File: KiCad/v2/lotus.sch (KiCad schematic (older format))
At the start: 32 parts, among them IC1 DW01A-G, J1 USB_OTG, J2 FTDI, Q1 FS8205A, SW1 SW_Push, SW2 SW_DIP_x01, SW3 SW_Push, U1 LD1117S33CTR, U2 TP4056, U3 ESP-12E

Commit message: Atualizado versão 2
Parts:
- removed BT1: Battery_Cell, Pin_Headers:Pin_Header_Straight_1x02_Pitch2.54mm, symbol Battery_Cell
- removed C1: 10u, Capacitors_SMD:C_0402, symbol C
- removed C2, C3: 0.1u, Capacitors_SMD:C_0402, symbol C
- removed C4, C5: 100n, Capacitors_SMD:C_0402, symbol C
- removed C6: 100n, Capacitors_Tantalum_SMD:CP_Tantalum_Case-C_EIA-6032-28_Hand, symbol CP1
- removed C7: 10u, Capacitors_Tantalum_SMD:CP_Tantalum_Case-C_EIA-6032-28_Hand, symbol CP1
- removed D1: LED_ARGB, LEDs:LED_D5.0mm-4, symbol LED_ARGB
- removed IC1: DW01A-G, DW01A-G:SOT95P190X145-6N, symbol DW01A-G
- removed J1: USB_OTG, Connectors:USB_Micro-B, symbol USB_OTG
- removed J2: FTDI, Pin_Headers:Pin_Header_Straight_1x04_Pitch2.54mm, symbol CONN_01X04
- removed Q1: FS8205A, FS8205A:SOP65P640X120-8N, symbol FS8205A
- removed R1, R2, R6: 1k, Resistors_SMD:R_0402, symbol R
- removed R10, R11, R12, R13, R4, R7, R8, R9: 10k, Resistors_SMD:R_0402, symbol R
- removed R3: 1.2k, Resistors_SMD:R_0402, symbol R
- removed R5: 100, Resistors_SMD:R_0402, symbol R
- removed SW1, SW3: SW_Push, Buttons_Switches_THT:SW_PUSH_6mm, symbol SW_Push
- removed SW2: SW_DIP_x01, Buttons_Switches_SMD:SW_DIP_x1_W5.08mm_Slide_Copal_CHS-A, symbol SW_DIP_x01-RESCUE-lotus
- removed U1: LD1117S33CTR, TO_SOT_Packages_SMD:SOT-223, symbol LD1117S33CTR
- removed U2: TP4056, TP4056:TP4056, symbol TP4056-RESCUE-lotus
- removed U3: ESP-12E, RF_Modules:ESP-12E, symbol ESP-12E
- added C? (x2): 100n, symbol Device:C
- added C?: 100n, symbol Device:CP1
- added C?: 10u, symbol Device:CP1
- added C?: 4.7u, symbol Device:C
- added C?: 1u, symbol Device:C
- added D?: LED_ARGB, symbol Device:LED_ARGB
- added J?: Conn_01x04, symbol Connector_Generic:Conn_01x04
- added J?: USB_B_Micro, symbol Connector:USB_B_Micro
- added R? (x6): 10k, symbol Device:R
- added R? (x2): 1.5k, symbol Device:R
- added R?: 1.13k, symbol Device:R
- added R?: 1.18k, symbol Device:R
- added SW? (x2): SW_Push, symbol Switch:SW_Push
- added SW?: SW_DIP_x01, symbol Switch:SW_DIP_x01
- added U?: ESP-12E, RF_Module:ESP-12E, symbol RF_Module:ESP-12E
- added U?: BQ24075, symbol Battery_Management:BQ24075
- added U?: LD1117S33TR_SOT223, Package_TO_SOT_SMD:SOT-223-3_TabPin2, symbol Regulator_Linear:LD1117S33TR_SOT223
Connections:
- net labels added: BAT, CHG, COLOR_BUTTON, LED_B, LED_G, LED_R, OUT, PGOOD, RST_BUTTON, TS_BAT
- net labels removed: LED_BUTTON, REST_BUTTON, led_b, led_g, led_r, pin_chrg, pin_stdby
- wire segments 103 -> 120
- no-connect marks 14 -> 7

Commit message: Adicionado bateria no esquemático v2
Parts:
- added C?: 4.7u, symbol Device:C
- added R?: 46.4k, symbol Device:R
- added R? (x2): 1.5k, symbol Device:R
- added U?: Battery, symbol Utils:Battery
- U?: value BQ24075 -> BQ24072; symbol Battery_Management:BQ24075 -> Battery_Management:BQ24072
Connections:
- wire segments 120 -> 136
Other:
- note added: "System"
- moved on the sheet: C?, D?, J?, R?, SW?, U?

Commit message: Mudado regulador de tensão
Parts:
- removed SW?: SW_DIP_x01, symbol Switch:SW_DIP_x01
- removed U?: LD1117S33TR_SOT223, Package_TO_SOT_SMD:SOT-223-3_TabPin2, symbol Regulator_Linear:LD1117S33TR_SOT223
- added J3: Conn_01x02, symbol Connector_Generic:Conn_01x02
- added U3: MIC5504-3.3YM5, Package_TO_SOT_SMD:SOT-23-5, symbol Regulator_Linear:MIC5504-3.3YM5
- C5: renamed from C?; value 100n -> 1u
- C6: renamed from C?; value 10u -> 1u
- gave numbers to parts that had none: 26
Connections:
- wire segments 136 -> 138
- no-connect marks 7 -> 11
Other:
- moved on the sheet: C5, C6

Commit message: Adicionado alguns footprints
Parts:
- C1, C2, C3, C4, C7: footprint (none) -> Capacitors_SMD:C_0402
- D1: footprint (none) -> LEDs:LED_Cree-PLCC4_3.2x2.8mm_CCW
- J1: footprint (none) -> Connectors:USB_Micro-B
- R1, R10, R11, R12, R13, R2, R3, R4, R5, R6, R7, R8, R9: footprint (none) -> Resistors_SMD:R_0402
- U1: footprint (none) -> Housings_DFN_QFN:QFN-16-1EP_3x3mm_Pitch0.5mm
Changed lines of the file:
@@
 F 0 "C1" H 2115 4846 50  0000 L CNN
 F 1 "100n" H 2115 4755 50  0000 L CNN
-F 2 "" H 2038 4650 50  0001 C CNN
+F 2 "Capacitors_SMD:C_0402" H 2038 4650 50  0001 C CNN
 F 3 "~" H 2000 4800 50  0001 C CNN
 	1    2000 4800
@@
 F 0 "R1" H 1870 4246 50  0000 L CNN
 F 1 "10k" H 1870 4155 50  0000 L CNN
-F 2 "" V 1730 4200 50  0001 C CNN
+F 2 "Resistors_SMD:R_0402" V 1730 4200 50  0001 C CNN
 F 3 "~" H 1800 4200 50  0001 C CNN
 	1    1800 4200
@@
 F 0 "R6" H 4120 4696 50  0000 L CNN
 F 1 "10k" H 4120 4605 50  0000 L CNN
-F 2 "" V 3980 4650 50  0001 C CNN
+F 2 "Resistors_SMD:R_0402" V 3980 4650 50  0001 C CNN
 F 3 "~" H 4050 4650 50  0001 C CNN
 	1    4050 4650
@@
 F 0 "R9" H 6520 5746 50  0000 L CNN
 F 1 "10k" H 6520 5655 50  0000 L CNN
-F 2 "" V 6380 5700 50  0001 C CNN
+F 2 "Resistors_SMD:R_0402" V 6380 5700 50  0001 C CNN
 F 3 "~" H 6450 5700 50  0001 C CNN
 	1    6450 5700
@@
 F 0 "R10" H 6570 4446 50  0000 L CNN
 F 1 "10k" H 6570 4355 50  0000 L CNN
-F 2 "" V 6430 4400 50  0001 C CNN
+F 2 "Resistors_SMD:R_0402" V 6430 4400 50  0001 C CNN
 F 3 "~" H 6500 4400 50  0001 C CNN
 	1    6500 4400
@@
 F 0 "R11" H 6920 4446 50  0000 L CNN
 F 1 "10k" H 6920 4355 50  0000 L CNN
-F 2 "" V 6780 4400 50  0001 C CNN
+F 2 "Resistors_SMD:R_0402" V 6780 4400 50  0001 C CNN
 F 3 "~" H 6850 4400 50  0001 C CNN
 	1    6850 4400
@@
 F 0 "D1" H 1800 6497 50  0000 C CNN
 F 1 "LED_ARGB" H 1800 6406 50  0000 C CNN
-F 2 "" H 1800 5950 50  0001 C CNN
+F 2 "LEDs:LED_Cree-PLCC4_3.2x2.8mm_CCW" H 1800 5950 50  0001 C CNN
 F 3 "~" H 1800 5950 50  0001 C CNN
 	1    1800 6000
@@
 F 0 "C3" H 3365 4846 50  0000 L CNN
 F 1 "100n" H 3365 4755 50  0000 L CNN
-F 2 "" H 3288 4650 50  0001 C CNN
+F 2 "Capacitors_SMD:C_0402" H 3288 4650 50  0001 C CNN
 F 3 "~" H 3250 4800 50  0001 C CNN
 	1    3250 4800
@@
 F 0 "R2" H 3120 4246 50  0000 L CNN
 F 1 "10k" H 3120 4155 50  0000 L CNN
-F 2 "" V 2980 4200 50  0001 C CNN
+F 2 "Resistors_SMD:R_0402" V 2980 4200 50  0001 C CNN
 F 3 "~" H 3050 4200 50  0001 C CNN
 	1    3050 4200
@@
 F 0 "U1" H 4400 2878 50  0000 C CNN
 F 1 "BQ24072" H 4400 2787 50  0000 C CNN
-F 2 "" H 4650 1550 50  0001 L CNN
+F 2 "Housings_DFN_QFN:QFN-16-1EP_3x3mm_Pitch0.5mm" H 4650 1550 50  0001 L CNN
 F 3 "http://www.ti.com/lit/ds/symlink/bq24075.pdf" H 4600 2300 50  0001 C CNN
 	1    4400 2100
@@
 F 0 "R7" V 5593 2400 50  0000 C CNN
 F 1 "1.5k" V 5684 2400 50  0000 C CNN
-F 2 "" V 5730 2400 50  0001 C CNN
+F 2 "Resistors_SMD:R_0402" V 5730 2400 50  0001 C CNN
 F 3 "~" H 5800 2400 50  0001 C CNN
 	1    5800 2400
@@
 F 0 "R8" V 5600 2500 50  0000 C CNN
 F 1 "1.5k" V 5700 2500 50  0000 C CNN
-F 2 "" V 5730 2500 50  0001 C CNN
+F 2 "Resistors_SMD:R_0402" V 5730 2500 50  0001 C CNN
 F 3 "~" H 5800 2500 50  0001 C CNN
 	1    5800 2500
@@
 F 0 "C4" H 5615 1946 50  0000 L CNN
 F 1 "4.7u" H 5615 1855 50  0000 L CNN
-F 2 "" H 5538 1750 50  0001 C CNN
+F 2 "Capacitors_SMD:C_0402" H 5538 1750 50  0001 C CNN
 F 3 "~" H 5500 1900 50  0001 C CNN
 	1    5500 1900
@@
 F 0 "C2" H 2600 2100 50  0000 L CNN
 F 1 "1u" H 2600 2000 50  0000 L CNN
-F 2 "" H 2838 1900 50  0001 C CNN
+F 2 "Capacitors_SMD:C_0402" H 2838 1900 50  0001 C CNN
 F 3 "~" H 2800 2050 50  0001 C CNN
 	1    2800 2050
@@
 F 0 "R5" H 3820 2796 50  0000 L CNN
 F 1 "1.13k" H 3820 2705 50  0000 L CNN
-F 2 "" V 3680 2750 50  0001 C CNN
+F 2 "Resistors_SMD:R_0402" V 3680 2750 50  0001 C CNN
 F 3 "~" H 3750 2750 50  0001 C CNN
 	1    3750 2750
@@
 F 0 "R4" H 3450 2800 50  0000 L CNN
 F 1 "1.18k" H 3350 2700 50  0000 L CNN
-F 2 "" V 3530 2750 50  0001 C CNN
+F 2 "Resistors_SMD:R_0402" V 3530 2750 50  0001 C CNN
 F 3 "~" H 3600 2750 50  0001 C CNN
 	1    3600 2750
@@
 F 0 "J1" H 2005 2417 50  0000 C CNN
 F 1 "USB_B_Micro" H 2005 2326 50  0000 C CNN
-F 2 "" H 2100 1900 50  0001 C CNN
+F 2 "Connectors:USB_Micro-B" H 2100 1900 50  0001 C CNN
 F 3 "~" H 2100 1900 50  0001 C CNN
 	1    1950 1950
@@
 F 0 "R3" H 3050 2200 50  0000 L CNN
 F 1 "46.4k" H 2950 2100 50  0000 L CNN
-F 2 "" V 3130 2150 50  0001 C CNN
+F 2 "Resistors_SMD:R_0402" V 3130 2150 50  0001 C CNN
 F 3 "~" H 3200 2150 50  0001 C CNN
 	1    3200 2150
@@
 F 0 "C7" H 9515 1696 50  0000 L CNN
 F 1 "4.7u" H 9515 1605 50  0000 L CNN
-F 2 "" H 9438 1500 50  0001 C CNN
+F 2 "Capacitors_SMD:C_0402" H 9438 1500 50  0001 C CNN
 F 3 "~" H 9400 1650 50  0001 C CNN
 	1    9400 1650
@@
 F 0 "R13" V 8650 2350 50  0000 C CNN
 F 1 "1.5k" V 8750 2350 50  0000 C CNN
-F 2 "" V 8780 2350 50  0001 C CNN
+F 2 "Resistors_SMD:R_0402" V 8780 2350 50  0001 C CNN
 F 3 "~" H 8850 2350 50  0001 C CNN
 	1    8850 2350
@@
 F 0 "R12" V 8350 2100 50  0000 C CNN
 F 1 "1.5k" V 8450 2100 50  0000 C CNN
-F 2 "" V 8480 2100 50  0001 C CNN
+F 2 "Resistors_SMD:R_0402" V 8480 2100 50  0001 C CNN
 F 3 "~" H 8550 2100 50  0001 C CNN
 	1    8550 2100

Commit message: Adicionado footprint dos botões, da bateria e dos conectores
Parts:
- C5, C6: footprint (none) -> Capacitors_Tantalum_SMD:CP_Tantalum_Case-A_EIA-3216-18_Hand
- J2: footprint (none) -> Connectors_JST:JST_JWPF_B04B-JWPF-SK-R_1x04_P2.00mm_Vertical
- SW1: footprint (none) -> Buttons_Switches_THT:SW_Tactile_SPST_Angled_PTS645Vx58-2LFS
- SW2: footprint (none) -> Buttons_Switches_THT:SW_PUSH_6mm
- U1: symbol Battery_Management:BQ24072 -> Lotus-rescue:BQ24072-Battery_Management
- U4: footprint (none) -> Pin_Headers:Pin_Header_Straight_1x03_Pitch2.54mm
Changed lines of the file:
@@
 EESchema Schematic File Version 4
 LIBS:Lotus-cache
-EELAYER 26 0
+EELAYER 29 0
 EELAYER END
 $Descr A4 11693 8268
@@
 F 0 "SW1" H 1800 4950 50  0000 R CNN
 F 1 "SW_Push" H 1750 4700 50  0000 R CNN
-F 2 "" H 1600 5000 50  0001 C CNN
+F 2 "Buttons_Switches_THT:SW_Tactile_SPST_Angled_PTS645Vx58-2LFS" H 1600 5000 50  0001 C CNN
 F 3 "" H 1600 5000 50  0001 C CNN
 	1    1600 4800
@@
 F 0 "SW2" H 3050 4950 50  0000 R CNN
 F 1 "SW_Push" H 3000 4700 50  0000 R CNN
-F 2 "" H 2850 5000 50  0001 C CNN
+F 2 "Buttons_Switches_THT:SW_PUSH_6mm" H 2850 5000 50  0001 C CNN
 F 3 "" H 2850 5000 50  0001 C CNN
 	1    2850 4800
@@
 F 0 "J2" H 2870 5575 50  0000 C CNN
 F 1 "Conn_01x04" H 2870 5666 50  0000 C CNN
-F 2 "" H 2950 6000 50  0001 C CNN
+F 2 "Connectors_JST:JST_JWPF_B04B-JWPF-SK-R_1x04_P2.00mm_Vertical" H 2950 6000 50  0001 C CNN
 F 3 "~" H 2950 6000 50  0001 C CNN
 	1    2950 6000
@@
 	2150 6000 2000 6000
 $Comp
-L Battery_Management:BQ24072 U1
+L Lotus-rescue:BQ24072-Battery_Management U1
 U 1 1 5BDC7AE2
 P 4400 2100
@@
 F 0 "C5" H 6665 2146 50  0000 L CNN
 F 1 "1u" H 6665 2055 50  0000 L CNN
-F 2 "" H 6550 2100 50  0001 C CNN
+F 2 "Capacitors_Tantalum_SMD:CP_Tantalum_Case-A_EIA-3216-18_Hand" H 6550 2100 50  0001 C CNN
 F 3 "~" H 6550 2100 50  0001 C CNN
 	1    6550 2100
@@
 F 0 "C6" H 7765 2146 50  0000 L CNN
 F 1 "1u" H 7765 2055 50  0000 L CNN
-F 2 "" H 7650 2100 50  0001 C CNN
+F 2 "Capacitors_Tantalum_SMD:CP_Tantalum_Case-A_EIA-3216-18_Hand" H 7650 2100 50  0001 C CNN
 F 3 "~" H 7650 2100 50  0001 C CNN
 	1    7650 2100
@@
 F 0 "U4" H 9477 2396 50  0000 L CNN
 F 1 "Battery" H 9477 2305 50  0000 L CNN
-F 2 "" H 9250 2300 50  0001 C CNN
+F 2 "Pin_Headers:Pin_Header_Straight_1x03_Pitch2.54mm" H 9250 2300 50  0001 C CNN
 F 3 "" H 9250 2300 50  0001 C CNN
 	1    9250 2300

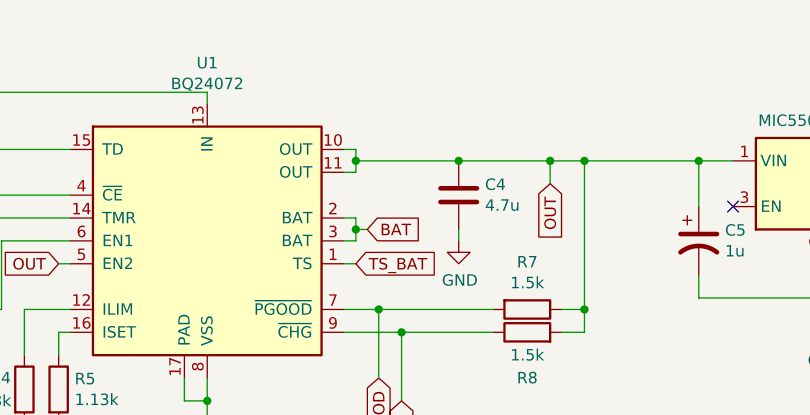
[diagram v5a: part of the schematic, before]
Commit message: Atualizado footprints
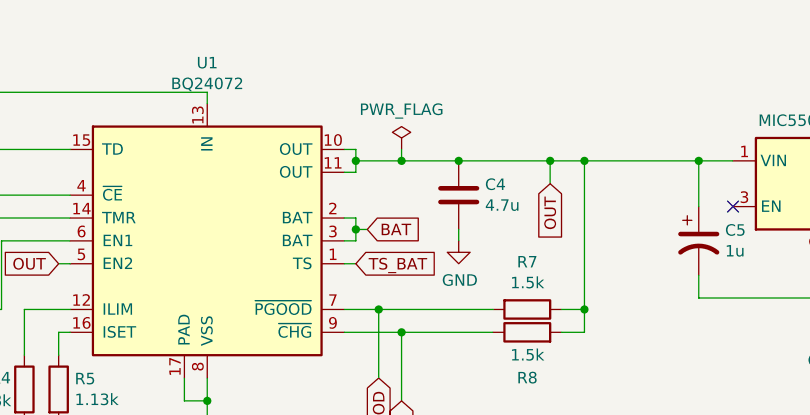
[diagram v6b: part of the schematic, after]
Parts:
- C1, C2, C3, C4, C7: footprint Capacitors_SMD:C_0402 -> Capacitor_SMD:C_0402_1005Metric
- C5, C6: footprint Capacitors_Tantalum_SMD:CP_Tantalum_Case-A_EIA-3216-18_Hand -> Capacitor_Tantalum_SMD:CP_EIA-3216-18_Kemet-A
- D1: footprint LEDs:LED_Cree-PLCC4_3.2x2.8mm_CCW -> LED_SMD:LED_Cree-PLCC4_3.2x2.8mm_CCW
- J1: footprint Connectors:USB_Micro-B -> Connector_USB:USB_Micro-B_Molex_47346-0001
- J2: footprint Connectors_JST:JST_JWPF_B04B-JWPF-SK-R_1x04_P2.00mm_Vertical -> Connector_PinHeader_2.54mm:PinHeader_1x04_P2.54mm_Vertical
- J3: footprint (none) -> Connector_PinHeader_2.54mm:PinHeader_1x02_P2.54mm_Vertical
- R1, R10, R11, R12, R13, R2, R3, R4, R5, R6, R7, R8, R9: footprint Resistors_SMD:R_0402 -> Resistor_SMD:R_0402_1005Metric
- SW1: footprint Buttons_Switches_THT:SW_Tactile_SPST_Angled_PTS645Vx58-2LFS -> Button_Switch_THT:SW_Tactile_SPST_Angled_PTS645Vx58-2LFS
- SW2: footprint Buttons_Switches_THT:SW_PUSH_6mm -> Button_Switch_THT:SW_PUSH_6mm
- U1: footprint Housings_DFN_QFN:QFN-16-1EP_3x3mm_Pitch0.5mm -> Package_DFN_QFN:QFN-16-1EP_3x3mm_P0.5mm_EP1.8x1.8mm
- U4: footprint Pin_Headers:Pin_Header_Straight_1x03_Pitch2.54mm -> Connector_PinHeader_2.54mm:PinHeader_1x03_P2.54mm_Vertical
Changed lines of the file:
@@
 EESchema Schematic File Version 4
-LIBS:Lotus-cache
-EELAYER 29 0
+LIBS:lotus-cache
+EELAYER 26 0
 EELAYER END
 $Descr A4 11693 8268
@@
 F 0 "SW1" H 1800 4950 50  0000 R CNN
 F 1 "SW_Push" H 1750 4700 50  0000 R CNN
-F 2 "Buttons_Switches_THT:SW_Tactile_SPST_Angled_PTS645Vx58-2LFS" H 1600 5000 50  0001 C CNN
+F 2 "Button_Switch_THT:SW_Tactile_SPST_Angled_PTS645Vx58-2LFS" H 1600 5000 50  0001 C CNN
 F 3 "" H 1600 5000 50  0001 C CNN
 	1    1600 4800
@@
 F 0 "C1" H 2115 4846 50  0000 L CNN
 F 1 "100n" H 2115 4755 50  0000 L CNN
-F 2 "Capacitors_SMD:C_0402" H 2038 4650 50  0001 C CNN
+F 2 "Capacitor_SMD:C_0402_1005Metric" H 2038 4650 50  0001 C CNN
 F 3 "~" H 2000 4800 50  0001 C CNN
 	1    2000 4800
@@
 F 0 "R1" H 1870 4246 50  0000 L CNN
 F 1 "10k" H 1870 4155 50  0000 L CNN
-F 2 "Resistors_SMD:R_0402" V 1730 4200 50  0001 C CNN
+F 2 "Resistor_SMD:R_0402_1005Metric" V 1730 4200 50  0001 C CNN
 F 3 "~" H 1800 4200 50  0001 C CNN
 	1    1800 4200
@@
 F 0 "R6" H 4120 4696 50  0000 L CNN
 F 1 "10k" H 4120 4605 50  0000 L CNN
-F 2 "Resistors_SMD:R_0402" V 3980 4650 50  0001 C CNN
+F 2 "Resistor_SMD:R_0402_1005Metric" V 3980 4650 50  0001 C CNN
 F 3 "~" H 4050 4650 50  0001 C CNN
 	1    4050 4650
@@
 F 0 "R9" H 6520 5746 50  0000 L CNN
 F 1 "10k" H 6520 5655 50  0000 L CNN
-F 2 "Resistors_SMD:R_0402" V 6380 5700 50  0001 C CNN
+F 2 "Resistor_SMD:R_0402_1005Metric" V 6380 5700 50  0001 C CNN
 F 3 "~" H 6450 5700 50  0001 C CNN
 	1    6450 5700
@@
 F 0 "R10" H 6570 4446 50  0000 L CNN
 F 1 "10k" H 6570 4355 50  0000 L CNN
-F 2 "Resistors_SMD:R_0402" V 6430 4400 50  0001 C CNN
+F 2 "Resistor_SMD:R_0402_1005Metric" V 6430 4400 50  0001 C CNN
 F 3 "~" H 6500 4400 50  0001 C CNN
 	1    6500 4400
@@
 F 0 "R11" H 6920 4446 50  0000 L CNN
 F 1 "10k" H 6920 4355 50  0000 L CNN
-F 2 "Resistors_SMD:R_0402" V 6780 4400 50  0001 C CNN
+F 2 "Resistor_SMD:R_0402_1005Metric" V 6780 4400 50  0001 C CNN
 F 3 "~" H 6850 4400 50  0001 C CNN
 	1    6850 4400
@@
 F 0 "D1" H 1800 6497 50  0000 C CNN
 F 1 "LED_ARGB" H 1800 6406 50  0000 C CNN
-F 2 "LEDs:LED_Cree-PLCC4_3.2x2.8mm_CCW" H 1800 5950 50  0001 C CNN
+F 2 "LED_SMD:LED_Cree-PLCC4_3.2x2.8mm_CCW" H 1800 5950 50  0001 C CNN
 F 3 "~" H 1800 5950 50  0001 C CNN
 	1    1800 6000
@@
 F 0 "SW2" H 3050 4950 50  0000 R CNN
 F 1 "SW_Push" H 3000 4700 50  0000 R CNN
-F 2 "Buttons_Switches_THT:SW_PUSH_6mm" H 2850 5000 50  0001 C CNN
+F 2 "Button_Switch_THT:SW_PUSH_6mm" H 2850 5000 50  0001 C CNN
 F 3 "" H 2850 5000 50  0001 C CNN
 	1    2850 4800
@@
 F 0 "C3" H 3365 4846 50  0000 L CNN
 F 1 "100n" H 3365 4755 50  0000 L CNN
-F 2 "Capacitors_SMD:C_0402" H 3288 4650 50  0001 C CNN
+F 2 "Capacitor_SMD:C_0402_1005Metric" H 3288 4650 50  0001 C CNN
 F 3 "~" H 3250 4800 50  0001 C CNN
 	1    3250 4800
@@
 F 0 "R2" H 3120 4246 50  0000 L CNN
 F 1 "10k" H 3120 4155 50  0000 L CNN
-F 2 "Resistors_SMD:R_0402" V 2980 4200 50  0001 C CNN
+F 2 "Resistor_SMD:R_0402_1005Metric" V 2980 4200 50  0001 C CNN
 F 3 "~" H 3050 4200 50  0001 C CNN
 	1    3050 4200
@@
 F 0 "J2" H 2870 5575 50  0000 C CNN
 F 1 "Conn_01x04" H 2870 5666 50  0000 C CNN
-F 2 "Connectors_JST:JST_JWPF_B04B-JWPF-SK-R_1x04_P2.00mm_Vertical" H 2950 6000 50  0001 C CNN
+F 2 "Connector_PinHeader_2.54mm:PinHeader_1x04_P2.54mm_Vertical" H 2950 6000 50  0001 C CNN
 F 3 "~" H 2950 6000 50  0001 C CNN
 	1    2950 6000
@@
 F 0 "U1" H 4400 2878 50  0000 C CNN
 F 1 "BQ24072" H 4400 2787 50  0000 C CNN
-F 2 "Housings_DFN_QFN:QFN-16-1EP_3x3mm_Pitch0.5mm" H 4650 1550 50  0001 L CNN
+F 2 "Package_DFN_QFN:QFN-16-1EP_3x3mm_P0.5mm_EP1.8x1.8mm" H 4650 1550 50  0001 L CNN
 F 3 "http://www.ti.com/lit/ds/symlink/bq24075.pdf" H 4600 2300 50  0001 C CNN
 	1    4400 2100
@@
 F 0 "R7" V 5593 2400 50  0000 C CNN
 F 1 "1.5k" V 5684 2400 50  0000 C CNN
-F 2 "Resistors_SMD:R_0402" V 5730 2400 50  0001 C CNN
+F 2 "Resistor_SMD:R_0402_1005Metric" V 5730 2400 50  0001 C CNN
 F 3 "~" H 5800 2400 50  0001 C CNN
 	1    5800 2400
@@
 F 0 "R8" V 5600 2500 50  0000 C CNN
 F 1 "1.5k" V 5700 2500 50  0000 C CNN
-F 2 "Resistors_SMD:R_0402" V 5730 2500 50  0001 C CNN
+F 2 "Resistor_SMD:R_0402_1005Metric" V 5730 2500 50  0001 C CNN
 F 3 "~" H 5800 2500 50  0001 C CNN
 	1    5800 2500
@@
 F 0 "C4" H 5615 1946 50  0000 L CNN
 F 1 "4.7u" H 5615 1855 50  0000 L CNN
-F 2 "Capacitors_SMD:C_0402" H 5538 1750 50  0001 C CNN
+F 2 "Capacitor_SMD:C_0402_1005Metric" H 5538 1750 50  0001 C CNN
 F 3 "~" H 5500 1900 50  0001 C CNN
 	1    5500 1900
@@
 F 0 "C5" H 6665 2146 50  0000 L CNN
 F 1 "1u" H 6665 2055 50  0000 L CNN
-F 2 "Capacitors_Tantalum_SMD:CP_Tantalum_Case-A_EIA-3216-18_Hand" H 6550 2100 50  0001 C CNN
+F 2 "Capacitor_Tantalum_SMD:CP_EIA-3216-18_Kemet-A" H 6550 2100 50  0001 C CNN
 F 3 "~" H 6550 2100 50  0001 C CNN
 	1    6550 2100
@@
 F 0 "C6" H 7765 2146 50  0000 L CNN
 F 1 "1u" H 7765 2055 50  0000 L CNN
-F 2 "Capacitors_Tantalum_SMD:CP_Tantalum_Case-A_EIA-3216-18_Hand" H 7650 2100 50  0001 C CNN
+F 2 "Capacitor_Tantalum_SMD:CP_EIA-3216-18_Kemet-A" H 7650 2100 50  0001 C CNN
 F 3 "~" H 7650 2100 50  0001 C CNN
 	1    7650 2100
@@
 Connection ~ 5500 1750
 Wire Wire Line
-	5500 1750 5050 1750
+	5500 1750 5250 1750
 Wire Wire Line
 	5500 2100 5500 2050
@@
 F 0 "C2" H 2600 2100 50  0000 L CNN
 F 1 "1u" H 2600 2000 50  0000 L CNN
-F 2 "Capacitors_SMD:C_0402" H 2838 1900 50  0001 C CNN
+F 2 "Capacitor_SMD:C_0402_1005Metric" H 2838 1900 50  0001 C CNN
 F 3 "~" H 2800 2050 50  0001 C CNN
 	1    2800 2050
@@
 F 0 "R5" H 3820 2796 50  0000 L CNN
 F 1 "1.13k" H 3820 2705 50  0000 L CNN
-F 2 "Resistors_SMD:R_0402" V 3680 2750 50  0001 C CNN
+F 2 "Resistor_SMD:R_0402_1005Metric" V 3680 2750 50  0001 C CNN
 F 3 "~" H 3750 2750 50  0001 C CNN
 	1    3750 2750
@@
 F 0 "R4" H 3450 2800 50  0000 L CNN
 F 1 "1.18k" H 3350 2700 50  0000 L CNN
-F 2 "Resistors_SMD:R_0402" V 3530 2750 50  0001 C CNN
+F 2 "Resistor_SMD:R_0402_1005Metric" V 3530 2750 50  0001 C CNN
 F 3 "~" H 3600 2750 50  0001 C CNN
 	1    3600 2750
@@
 F 0 "J1" H 2005 2417 50  0000 C CNN
 F 1 "USB_B_Micro" H 2005 2326 50  0000 C CNN
-F 2 "Connectors:USB_Micro-B" H 2100 1900 50  0001 C CNN
+F 2 "Connector_USB:USB_Micro-B_Molex_47346-0001" H 2100 1900 50  0001 C CNN
 F 3 "~" H 2100 1900 50  0001 C CNN
 	1    1950 1950
@@
 F 0 "R3" H 3050 2200 50  0000 L CNN
 F 1 "46.4k" H 2950 2100 50  0000 L CNN
-F 2 "Resistors_SMD:R_0402" V 3130 2150 50  0001 C CNN
+F 2 "Resistor_SMD:R_0402_1005Metric" V 3130 2150 50  0001 C CNN
 F 3 "~" H 3200 2150 50  0001 C CNN
 	1    3200 2150
@@
 F 0 "U4" H 9477 2396 50  0000 L CNN
 F 1 "Battery" H 9477 2305 50  0000 L CNN
-F 2 "Pin_Headers:Pin_Header_Straight_1x03_Pitch2.54mm" H 9250 2300 50  0001 C CNN
+F 2 "Connector_PinHeader_2.54mm:PinHeader_1x03_P2.54mm_Vertical" H 9250 2300 50  0001 C CNN
 F 3 "" H 9250 2300 50  0001 C CNN
 	1    9250 2300
@@
 F 0 "C7" H 9515 1696 50  0000 L CNN
 F 1 "4.7u" H 9515 1605 50  0000 L CNN
-F 2 "Capacitors_SMD:C_0402" H 9438 1500 50  0001 C CNN
+F 2 "Capacitor_SMD:C_0402_1005Metric" H 9438 1500 50  0001 C CNN
 F 3 "~" H 9400 1650 50  0001 C CNN
 	1    9400 1650
@@
 F 0 "R13" V 8650 2350 50  0000 C CNN
 F 1 "1.5k" V 8750 2350 50  0000 C CNN
-F 2 "Resistors_SMD:R_0402" V 8780 2350 50  0001 C CNN
+F 2 "Resistor_SMD:R_0402_1005Metric" V 8780 2350 50  0001 C CNN
 F 3 "~" H 8850 2350 50  0001 C CNN
 	1    8850 2350
@@
 F 0 "R12" V 8350 2100 50  0000 C CNN
 F 1 "1.5k" V 8450 2100 50  0000 C CNN
-F 2 "Resistors_SMD:R_0402" V 8480 2100 50  0001 C CNN
+F 2 "Resistor_SMD:R_0402_1005Metric" V 8480 2100 50  0001 C CNN
 F 3 "~" H 8550 2100 50  0001 C CNN
 	1    8550 2100
@@
 F 0 "J3" H 7380 4642 50  0000 L CNN
 F 1 "Conn_01x02" H 7380 4551 50  0000 L CNN
-F 2 "" H 7300 4650 50  0001 C CNN
+F 2 "Connector_PinHeader_2.54mm:PinHeader_1x02_P2.54mm_Vertical" H 7300 4650 50  0001 C CNN
 F 3 "~" H 7300 4650 50  0001 C CNN
 	1    7300 4650
@@
 NoConn ~ 2250 1950
 NoConn ~ 1850 2350
+$Comp
+L power:PWR_FLAG #FLG0103
+U 1 1 5C075C87
+P 5250 1700
+F 0 "#FLG0103" H 5250 1775 50  0001 C CNN
+F 1 "PWR_FLAG" H 5250 1874 50  0000 C CNN
+F 2 "" H 5250 1700 50  0001 C CNN
+F 3 "~" H 5250 1700 50  0001 C CNN
+	1    5250 1700
+	1    0    0    -1
+$EndComp
+Wire Wire Line
+	5250 1700 5250 1750
+Connection ~ 5250 1750
+Wire Wire Line
+	5250 1750 5050 1750
 $EndSCHEMATC
